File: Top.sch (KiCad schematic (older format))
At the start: 0 parts

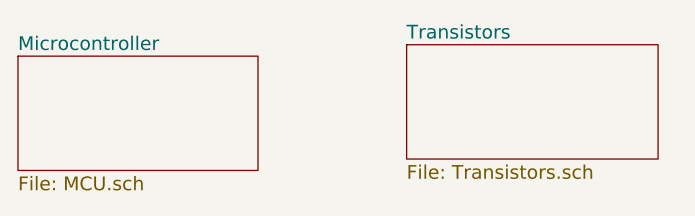
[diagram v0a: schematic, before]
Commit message: Added Multiwatt15 footprint to L298
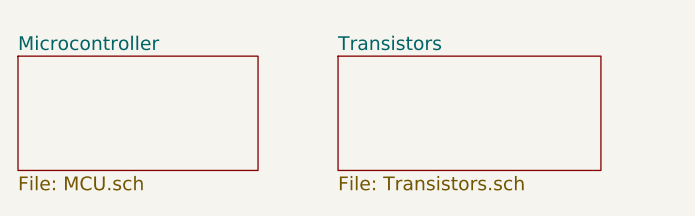
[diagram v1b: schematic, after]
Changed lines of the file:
@@
 EESchema Schematic File Version 2
+LIBS:L298
 LIBS:power
 LIBS:device
@@
 $Descr A4 11693 8268
 encoding utf-8
-Sheet 1 4
+Sheet 1 8
 Title ""
 Date ""
@@
 $EndSheet
 $Sheet
-S 4050 2200 1100 500
+S 3750 2250 1150 500
 U 5A23F11B
 F0 "Transistors" 60
